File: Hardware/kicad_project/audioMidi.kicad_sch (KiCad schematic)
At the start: 49 parts, among them J3 line_in, J4 headphone_out, J5 midi_in, J6 midi_out, U3 TLV320AIC3204, U4 AP3722AT_mic, U5 6N137, U7 apx804SR, U8 LM4890, U9 ME6211C

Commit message: v9 hardware
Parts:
- removed C4, C66: 1u, Capacitors_Tantalum_SMD:CP_Tantalum_Case-A_EIA-3216-18_Reflow, symbol Device:CP1
- removed C65, C67: 470nf, Capacitors_Tantalum_SMD:CP_Tantalum_Case-A_EIA-3216-18_Reflow, symbol Device:CP1
- removed JP7, JP8: SolderJumper_2_Bridged, Jumper:SolderJumper-2_P1.3mm_Bridged_Pad1.0x1.5mm, symbol Jumper:SolderJumper_2_Bridged
- removed LS1: Speaker, Connector_PinHeader_2.54mm:PinHeader_1x02_P2.54mm_Horizontal, symbol Device:Speaker
- removed R21, R22, R23, R30: 20k, Resistors_SMD:R_0402_NoSilk, symbol Device:R
- removed U7: apx804SR, TO_SOT_Packages_SMD:SOT-23, symbol customLibrary:apx804SR
- removed U8: LM4890, Housings_SSOP:MSOP-8_3x3mm_Pitch0.65mm, symbol customLibrary:fm8002a
- added D26, D3, D4, D5: D_Zener, Diode_SMD:D_SOD-323F, symbol Device:D_Zener
- added JP15, JP18: SolderJumper_2_Bridged, Jumper:SolderJumper-2_P1.3mm_Bridged_Pad1.0x1.5mm, symbol Jumper:SolderJumper_2_Bridged
- added JP16, JP17: SolderJumper_2_Open, Jumper:SolderJumper-2_P1.3mm_Open_RoundedPad1.0x1.5mm, symbol Jumper:SolderJumper_2_Open
- added R32, R33: 100, Resistor_SMD:R_01005_0402Metric, symbol Device:R
- C39, C44, C45, C47: LCSC c1623 -> C1623
- C48, C49: LCSC C96123 -> C96123
- D52: LCSC c2128 -> C2128
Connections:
- net +3V3A: no longer R14.1
- net GND: now also R14.1, D26.2 (A), D3.2 (A)
- net at C39.2, R24.1: now also D4.2 (A), JP16.2 (B), R32.1; no longer J3.2 (TIP_1)
- net at C44.2: now also D5.2 (A), JP17.2 (B), R33.1; no longer J3.3 (RING)
- new net: J3.2 (TIP_1), JP15.2 (B), JP16.1 (A)
- new net: J3.3 (RING), JP17.1 (A), JP18.2 (B)
- new net: D3.1 (K), D4.1 (K)
- new net: JP15.1 (A), R32.2
- new net: JP18.1 (A), R33.2
- new net: D26.1 (K), D5.1 (K)
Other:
- moved on the sheet: C38, C39, C40, C41, C42, C43, C44, C45, C46, C47, C48, C49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

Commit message: v10 board
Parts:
- removed C50: 10u, Capacitors_SMD:C_0402_NoSilk, symbol Device:C
- removed D52: D, RandomJunk:D_SOD-323F_less_silk, symbol Device:D
- removed JP15, JP18: SolderJumper_2_Bridged, Jumper:SolderJumper-2_P1.3mm_Bridged_Pad1.0x1.5mm, symbol Jumper:SolderJumper_2_Bridged
- removed JP16, JP17: SolderJumper_2_Open, Jumper:SolderJumper-2_P1.3mm_Open_RoundedPad1.0x1.5mm, symbol Jumper:SolderJumper_2_Open
- removed U5: 6N137, RandomJunk:SOP-8_3.9x5.1x1.27P, symbol dk_Optoisolators-Logic-Output:6N137
- added C4: 10u, Capacitor_SMD:C_0402_1005Metric, symbol Device:C
- added R21: 220, Resistor_SMD:R_0402_1005Metric, symbol Device:R
- added U5: HCPL-0631, Package_SO:SOIC-8_3.9x4.9mm_P1.27mm, symbol Isolator:HCPL-0631
- C38, C40, C41, C42, C43, C46, C5, C63: footprint Capacitors_SMD:C_0402_NoSilk -> Capacitor_SMD:C_0402_1005Metric; checked (none) -> 1
- C39, C44, C45, C47, C48, C49, C58, D26, D3, D4, D5, R32, R33, U3, U4: checked (none) -> 1
- J3, J4, J5, J6: Field4 CUI Inc -> (none); Field5 1.01 -> (none)
- JP1, JP2, JP3, JP4: checked 1 -> (none)
- R10, R14, R24, R9: footprint Resistors_SMD:R_0402_NoSilk -> Resistor_SMD:R_0402_1005Metric; checked (none) -> 1
- R11: value 1k -> 220; footprint Resistors_SMD:R_0402_NoSilk -> Resistor_SMD:R_0402_1005Metric; LCSC C11702 -> C25091; checked (none) -> 1
- R12: value 220 -> 33; footprint Resistors_SMD:R_0402_NoSilk -> Resistor_SMD:R_0402_1005Metric; LCSC C25091 -> C25105; checked (none) -> 1
- R13: value 220 -> 10; footprint Resistors_SMD:R_0402_NoSilk -> Resistor_SMD:R_0402_1005Metric; LCSC C25091 -> C25077; checked (none) -> 1
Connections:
- net +3V3: now also R10.2, C4.1, U5.8 (VCC); no longer R11.2
- net GND: now also C4.2, U5.5 (GND)
- net MIDI_RX: now also R10.1, U5.6 (VO2), U5.7 (VO1); no longer R11.1
- net at J3.2 (TIP_1): now also R32.2
- net at J3.3 (RING): now also R33.2
- net at J5.2 (TIP_1): now also R21.1, U5.2 (C1)
- net at J5.3 (RING): now also R11.1, U5.3 (C2); no longer R10.2
- new net: R11.2, U5.1 (A1)
- new net: R21.2, U5.4 (A2)
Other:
- note added: "2014 midi spec tells us to use lower resistance when on 3v3"
- note added: "auto crossover midi input by kay (lpzw modules)"
- moved on the sheet: C5, C58, C63, D26, D3, D4, D5, J6, R12, R13, R32, R33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

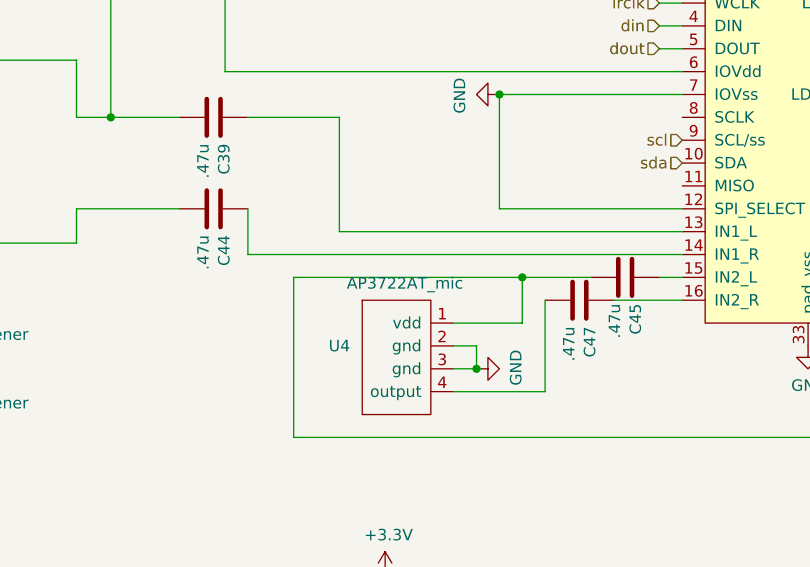
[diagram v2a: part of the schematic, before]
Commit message: pcb bodge fixes
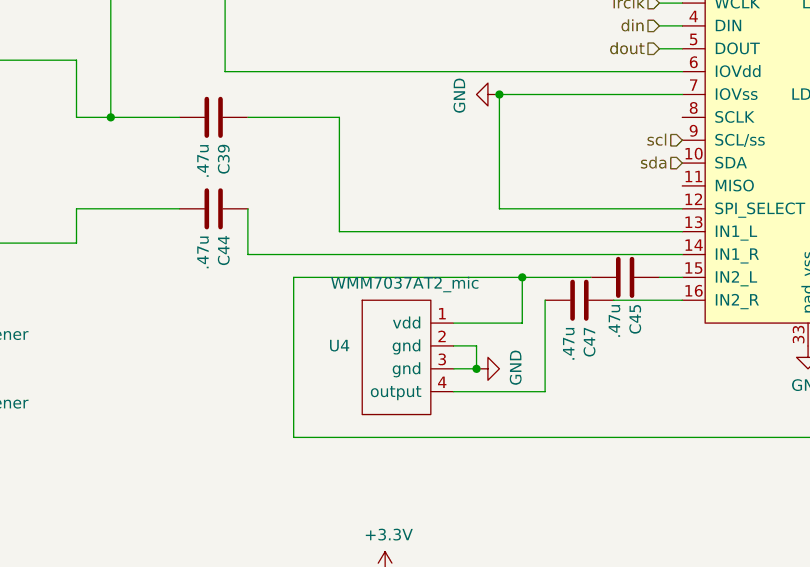
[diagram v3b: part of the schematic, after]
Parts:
- U4: value AP3722AT_mic -> WMM7037AT2_mic; footprint RandomJunk:AP3722AT-SMD-mic -> MyLibrary:LGA-4(3x3.8); LCSC C918198 -> C140705
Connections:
- net VBUS renamed VSYS
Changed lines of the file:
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@@
     (in_bom yes) (on_board yes)
     (property "Reference" "U4" (id 0) (at 110.49 86.36 0))
-    (property "Value" "AP3722AT_mic" (id 1) (at 117.7798 79.4004 0))
-    (property "Footprint" "RandomJunk:AP3722AT-SMD-mic" (id 2) (at 113.03 81.28 0)
+    (property "Value" "WMM7037AT2_mic" (id 1) (at 117.7798 79.4004 0))
+    (property "Footprint" "MyLibrary:LGA-4(3x3.8)" (id 2) (at 113.03 81.28 0)
       (effects (font (size 1.27 1.27)) hide)
     )
@@
       (effects (font (size 1.27 1.27)) hide)
     )
-    (property "LCSC" "C918198" (id 4) (at 116.84 86.36 0)
+    (property "LCSC" "C140705" (id 4) (at 116.84 86.36 0)
       (effects (font (size 1.27 1.27)) hide)
     )
@@
     (pin "1")
     (pin "2")
-  )
-  (symbol (lib_id "customLibrary:VSYS") (at 223.52 134.62 0) (unit 1)
-    (in_bom yes) (on_board yes)
-    (property "Reference" "#PWR0111" (id 0) (at 223.52 138.43 0)
-      (effects (font (size 1.27 1.27)) hide)
-    )
-    (property "Value" "VSYS" (id 1) (at 223.901 130.2258 0))
-    (property "Footprint" "" (id 2) (at 223.52 134.62 0)
-      (effects (font (size 1.27 1.27)) hide)
-    )
-    (property "Datasheet" "" (id 3) (at 223.52 134.62 0)
-      (effects (font (size 1.27 1.27)) hide)
-    )
-    (pin "1")
   )
   (symbol (lib_id "customLibrary:+3V3A") (at 269.24 129.54 0) (unit 1)
@@
     (pin "2")
   )
+  (symbol (lib_name "VSYS_1") (lib_id "customLibrary:VSYS") (at 223.52 134.62 0) (unit 1)
+    (in_bom yes) (on_board yes)
+    (property "Reference" "#PWR0111" (id 0) (at 223.52 138.43 0)
+      (effects (font (size 1.27 1.27)) hide)
+    )
+    (property "Value" "VSYS" (id 1) (at 223.901 130.2258 0))
+    (property "Footprint" "" (id 2) (at 223.52 134.62 0)
+      (effects (font (size 1.27 1.27)) hide)
+    )
+    (property "Datasheet" "" (id 3) (at 223.52 134.62 0)
+      (effects (font (size 1.27 1.27)) hide)
+    )
+    (pin "1")
+  )
   (symbol (lib_id "Device:C") (at 120.65 118.11 0) (unit 1)
